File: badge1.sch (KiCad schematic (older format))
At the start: 23 parts, among them P1 CONN_01X04, P2 USB_A, P3 CONN_01X04, P4 CONN_01X03, SW1 SW_PUSH, U1 MCP1700-3302E/TO, U2 custom_logo, U3 Hillhacks_logo, U4 proto_area, U5 badge_hole2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

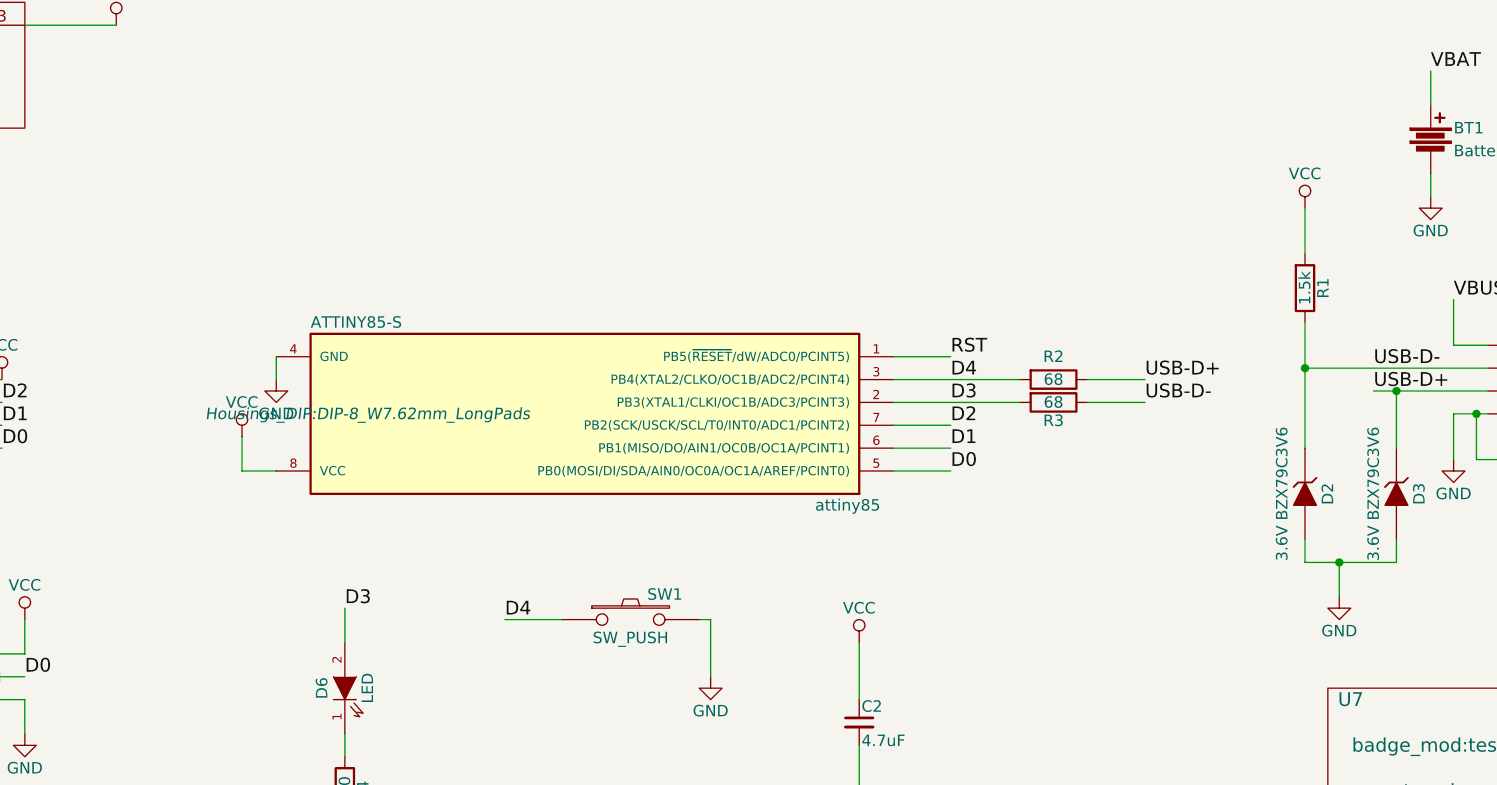
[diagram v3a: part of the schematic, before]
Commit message: fixed mistakes and made button the reset button. added more legend.
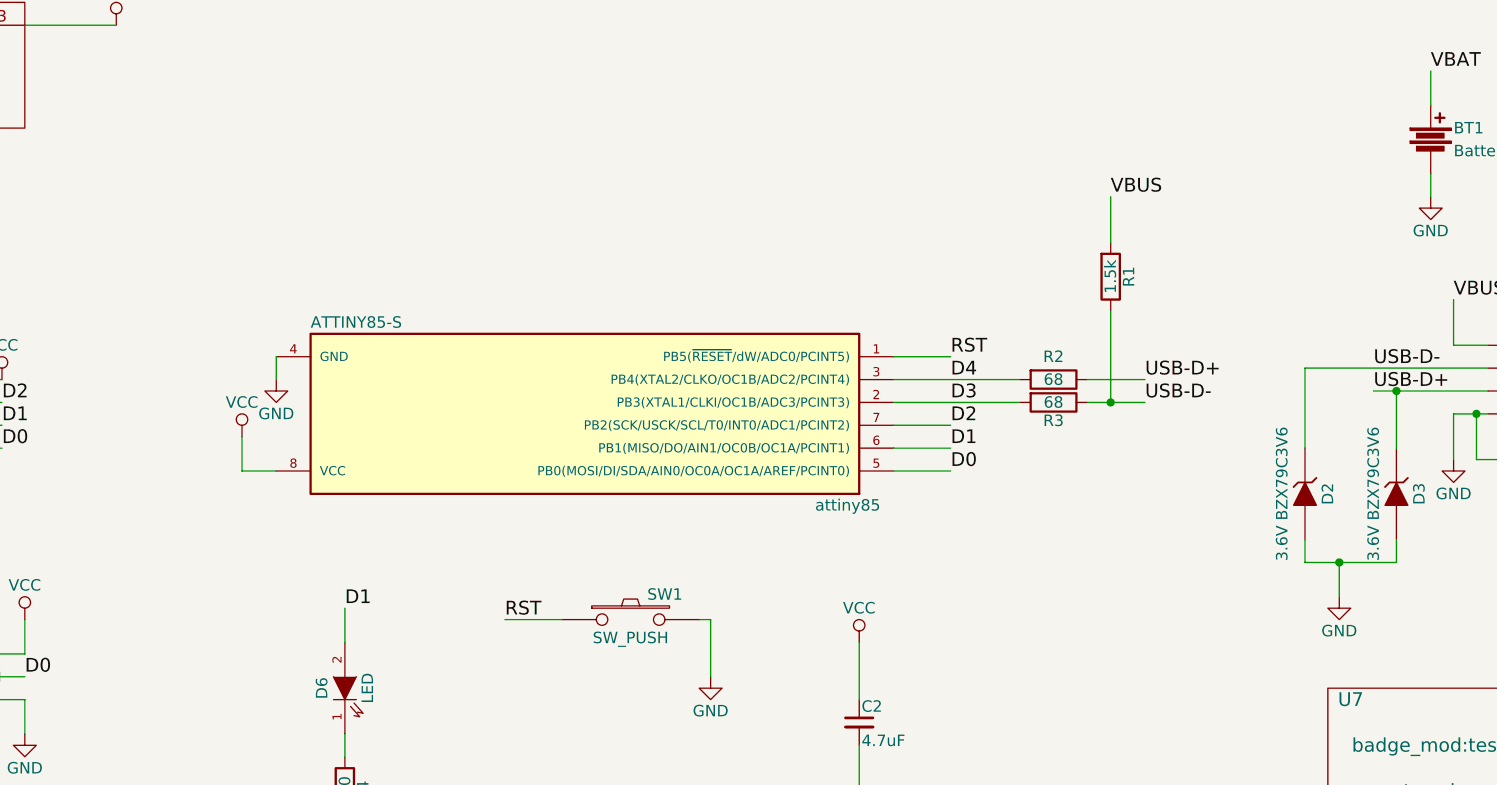
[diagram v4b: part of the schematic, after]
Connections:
- net D1: now also D6.2 (A)
- net D3: no longer D6.2 (A)
- net D4: no longer SW1.1
- net RST: now also SW1.1
- net VBUS: now also R1.2
- net VCC: no longer R1.2
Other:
- moved on the sheet: R1
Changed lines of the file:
@@
 F 0 "attiny85" H 3700 4150 50  0000 C CNN
 F 1 "ATTINY85-S" H 5850 3350 50  0000 C CNN
-F 2 "Housings_DIP:DIP-8_W7.62mm_LongPads" H 5800 3750 50  0000 C CIN
+F 2 "Housings_DIP:DIP-8_W7.62mm_LongPads" H 5800 3750 50  0001 C CIN
 F 3 "" H 4850 3750 50  0001 C CNN
 F 4 "ATTINY85-20SURCT-ND" H 4850 3750 60  0001 C CNN "digikey"
@@
 $EndComp
 Text Label 3800 4600 0    60   ~ 0
-D3
+D1
 $Comp
 L GND #PWR011
@@
 	1    0    0    -1
 $EndComp
-Text Label 4500 4650 0    60   ~ 0
-D4
 $Comp
 L SW_PUSH SW1
@@
 L R R1
 U 1 1 56D7518A
-P 8000 3200
-F 0 "R1" V 8080 3200 50  0000 C CNN
-F 1 "1.5k" V 8000 3200 50  0000 C CNN
-F 2 "Resistors_ThroughHole:Resistor_Horizontal_RM10mm" V 7930 3200 50  0001 C CNN
-F 3 "" H 8000 3200 50  0000 C CNN
-	1    8000 3200
+P 7150 3150
+F 0 "R1" V 7230 3150 50  0000 C CNN
+F 1 "1.5k" V 7150 3150 50  0000 C CNN
+F 2 "Resistors_ThroughHole:Resistor_Horizontal_RM10mm" V 7080 3150 50  0001 C CNN
+F 3 "" H 7150 3150 50  0000 C CNN
+	1    7150 3150
 	1    0    0    1
 $EndComp
-$Comp
-L VCC #PWR015
-U 1 1 56D755A1
-P 8000 2850
-F 0 "#PWR015" H 8000 2700 50  0001 C CNN
-F 1 "VCC" H 8000 3000 50  0000 C CNN
-F 2 "" H 8000 2850 50  0000 C CNN
-F 3 "" H 8000 2850 50  0000 C CNN
-	1    8000 2850
-	1    0    0    -1
-$EndComp
-Wire Wire Line
-	8000 2850 8000 3050
-Connection ~ 8000 3550
-Wire Wire Line
-	8000 4400 8000 4300
-Wire Wire Line
-	2300 3900 2100 3900
-Wire Wire Line
-	8550 2800 8550 2700
-Wire Wire Line
-	8550 2250 8550 2400
-Wire Wire Line
-	2300 3700 2100 3700
-Wire Wire Line
-	1000 3900 1200 3900
-Wire Wire Line
-	1200 3800 1000 3800
-Wire Wire Line
-	1000 3700 1200 3700
-Wire Wire Line
-	1200 3600 1000 3600
-Wire Wire Line
-	2300 3600 2100 3600
-Wire Wire Line
-	2100 3800 2300 3800
-Wire Wire Line
-	4500 4650 4750 4650
-Wire Wire Line
-	5400 4900 5400 4650
-Wire Wire Line
-	5400 4650 5350 4650
-Wire Wire Line
-	3800 5250 3800 5150
-Wire Wire Line
-	3800 5700 3800 5550
-Wire Wire Line
-	3800 4600 3800 4750
-Connection ~ 8750 3750
-Wire Wire Line
-	8750 3950 8750 3750
-Wire Wire Line
-	9200 3950 8750 3950
-Wire Wire Line
-	6050 4750 6050 5000
-Wire Wire Line
-	6050 5200 6050 5500
-Wire Wire Line
-	1150 5000 1750 5000
-Wire Wire Line
-	1150 4900 1750 4900
-Wire Wire Line
-	1150 4800 1750 4800
-Wire Wire Line
-	2400 4800 2000 4800
-Wire Wire Line
-	2400 4650 2400 4800
-Wire Wire Line
-	2400 5000 2000 5000
-Wire Wire Line
-	2400 5150 2400 5000
-Wire Wire Line
-	2400 4900 2000 4900
-Connection ~ 8400 3650
-Wire Wire Line
-	8400 3900 8400 3650
-Wire Wire Line
-	8000 3350 8000 3900
-Connection ~ 8150 4400
-Wire Wire Line
-	8400 4400 8400 4300
-Wire Wire Line
-	8150 4400 8150 4550
-Wire Wire Line
-	8000 4400 8400 4400
-Wire Wire Line
-	6200 3600 6750 3600
-Wire Wire Line
-	6200 3700 6750 3700
-Wire Wire Line
-	6450 3900 6200 3900
-Wire Wire Line
-	7300 3600 7050 3600
-Wire Wire Line
-	7300 3700 7050 3700
-Wire Wire Line
-	8300 3650 8800 3650
-Wire Wire Line
-	8000 3550 8800 3550
-Wire Wire Line
-	8650 3750 8800 3750
-Wire Wire Line
-	8650 3950 8650 3750
-Wire Wire Line
-	8650 3450 8800 3450
-Wire Wire Line
-	8650 3250 8650 3450
-Wire Wire Line
-	3500 3600 3500 3500
-Wire Wire Line
-	3350 4000 3500 4000
-Wire Wire Line
-	3350 3850 3350 4000
-Wire Wire Line
-	6450 3500 6200 3500
-Wire Wire Line
-	6200 4000 6450 4000
-Wire Wire Line
-	6450 3800 6200 3800
 $Comp
 L CONN_01X03 P4
@@
 	1    0    0    -1
 $EndComp
-Wire Wire Line
-	9900 3200 10250 3200
-Wire Wire Line
-	9900 3000 10250 3000
-Wire Wire Line
-	9500 3050 9500 3100
-Wire Wire Line
-	9500 3100 10250 3100
 $Comp
 L MCP1700-3302E/TO U1
@@
 $EndComp
 $Comp
-L VCC #PWR016
+L VCC #PWR015
 U 1 1 56D86F61
 P 2800 2050
-F 0 "#PWR016" H 2800 1900 50  0001 C CNN
+F 0 "#PWR015" H 2800 1900 50  0001 C CNN
 F 1 "VCC" H 2800 2200 50  0000 C CNN
 F 2 "" H 2800 2050 50  0000 C CNN
@@
 $EndComp
 $Comp
-L GND #PWR017
+L GND #PWR016
 U 1 1 56D86FA3
 P 2000 2650
-F 0 "#PWR017" H 2000 2400 50  0001 C CNN
+F 0 "#PWR016" H 2000 2400 50  0001 C CNN
 F 1 "GND" H 2000 2500 50  0000 C CNN
 F 2 "" H 2000 2650 50  0000 C CNN
@@
 Text Label 850  2050 0    60   ~ 0
 V_sec_bat
-Wire Wire Line
-	850  2050 1600 2050
-Wire Wire Line
-	2400 2050 2800 2050
-Wire Wire Line
-	2000 2500 2000 2650
 Text Label 1700 1050 0    60   ~ 0
 V_sec_bat
-Wire Wire Line
-	1700 1050 1600 1050
-$Comp
-L GND #PWR018
+$Comp
+L GND #PWR017
 U 1 1 56D87B87
 P 2950 1050
-F 0 "#PWR018" H 2950 800 50  0001 C CNN
+F 0 "#PWR017" H 2950 800 50  0001 C CNN
 F 1 "GND" H 2950 900 50  0000 C CNN
 F 2 "" H 2950 1050 50  0000 C CNN
@@
 	1    0    0    -1
 $EndComp
-Wire Wire Line
-	2950 1050 2700 1050
 $Comp
 L badge_hole2 U5
@@
 	1    0    0    -1
 $EndComp
+Text Label 7150 2800 0    60   ~ 0
+VBUS
+Wire Wire Line
+	7150 2800 7150 3000
+Wire Wire Line
+	8000 4400 8000 4300
+Wire Wire Line
+	2300 3900 2100 3900
+Wire Wire Line
+	8550 2800 8550 2700
+Wire Wire Line
+	8550 2250 8550 2400
+Wire Wire Line
+	2300 3700 2100 3700
+Wire Wire Line
+	1000 3900 1200 3900
+Wire Wire Line
+	1200 3800 1000 3800
+Wire Wire Line
+	1000 3700 1200 3700
+Wire Wire Line
+	1200 3600 1000 3600
+Wire Wire Line
+	2300 3600 2100 3600
+Wire Wire Line
+	2100 3800 2300 3800
+Wire Wire Line
+	4500 4650 4750 4650
+Wire Wire Line
+	5400 4900 5400 4650
+Wire Wire Line
+	5400 4650 5350 4650
+Wire Wire Line
+	3800 5250 3800 5150
+Wire Wire Line
+	3800 5700 3800 5550
+Wire Wire Line
+	3800 4600 3800 4750
+Connection ~ 8750 3750
+Wire Wire Line
+	8750 3950 8750 3750
+Wire Wire Line
+	9200 3950 8750 3950
+Wire Wire Line
+	6050 4750 6050 5000
+Wire Wire Line
+	6050 5200 6050 5500
+Wire Wire Line
+	1150 5000 1750 5000
+Wire Wire Line
+	1150 4900 1750 4900
+Wire Wire Line
+	1150 4800 1750 4800
+Wire Wire Line
+	2400 4800 2000 4800
+Wire Wire Line
+	2400 4650 2400 4800
+Wire Wire Line
+	2400 5000 2000 5000
+Wire Wire Line
+	2400 5150 2400 5000
+Wire Wire Line
+	2400 4900 2000 4900
+Connection ~ 8400 3650
+Wire Wire Line
+	8400 3900 8400 3650
+Connection ~ 8150 4400
+Wire Wire Line
+	8400 4400 8400 4300
+Wire Wire Line
+	8150 4400 8150 4550
+Wire Wire Line
+	8000 4400 8400 4400
+Wire Wire Line
+	6200 3600 6750 3600
+Wire Wire Line
+	6200 3700 6750 3700
+Wire Wire Line
+	6450 3900 6200 3900
+Wire Wire Line
+	7300 3600 7050 3600
+Wire Wire Line
+	7300 3700 7050 3700
+Wire Wire Line
+	8300 3650 8800 3650
+Wire Wire Line
+	8000 3550 8800 3550
+Wire Wire Line
+	8650 3750 8800 3750
+Wire Wire Line
+	8650 3950 8650 3750
+Wire Wire Line
+	8650 3450 8800 3450
+Wire Wire Line
+	8650 3250 8650 3450
+Wire Wire Line
+	3500 3600 3500 3500
+Wire Wire Line
+	3350 4000 3500 4000
+Wire Wire Line
+	3350 3850 3350 4000
+Wire Wire Line
+	6450 3500 6200 3500
+Wire Wire Line
+	6200 4000 6450 4000
+Wire Wire Line
+	6450 3800 6200 3800
+Wire Wire Line
+	9900 3200 10250 3200
+Wire Wire Line
+	9900 3000 10250 3000
+Wire Wire Line
+	9500 3050 9500 3100
+Wire Wire Line
+	9500 3100 10250 3100
+Wire Wire Line
+	850  2050 1600 2050
+Wire Wire Line
+	2400 2050 2800 2050
+Wire Wire Line
+	2000 2500 2000 2650
+Wire Wire Line
+	1700 1050 1600 1050
+Wire Wire Line
+	2950 1050 2700 1050
+Wire Wire Line
+	8000 3550 8000 3900
+Wire Wire Line
+	7150 3700 7150 3300
+Connection ~ 7150 3700
+Text Label 4500 4650 0    60   ~ 0
+RST
 $EndSCHEMATC

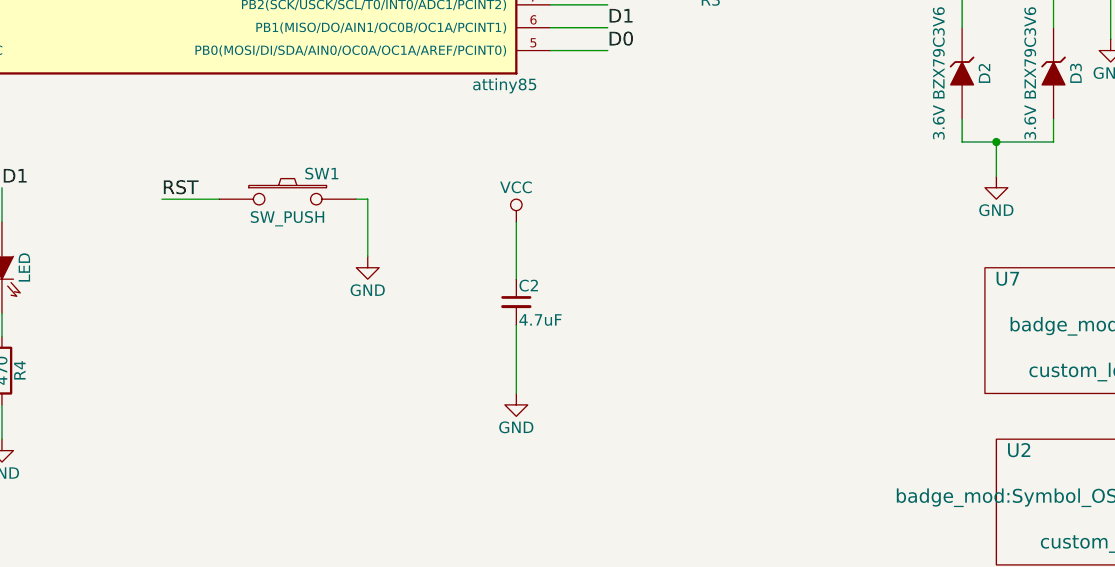
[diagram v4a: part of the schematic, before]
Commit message: Update schematic/layout with fixes. Update readme for small howto.
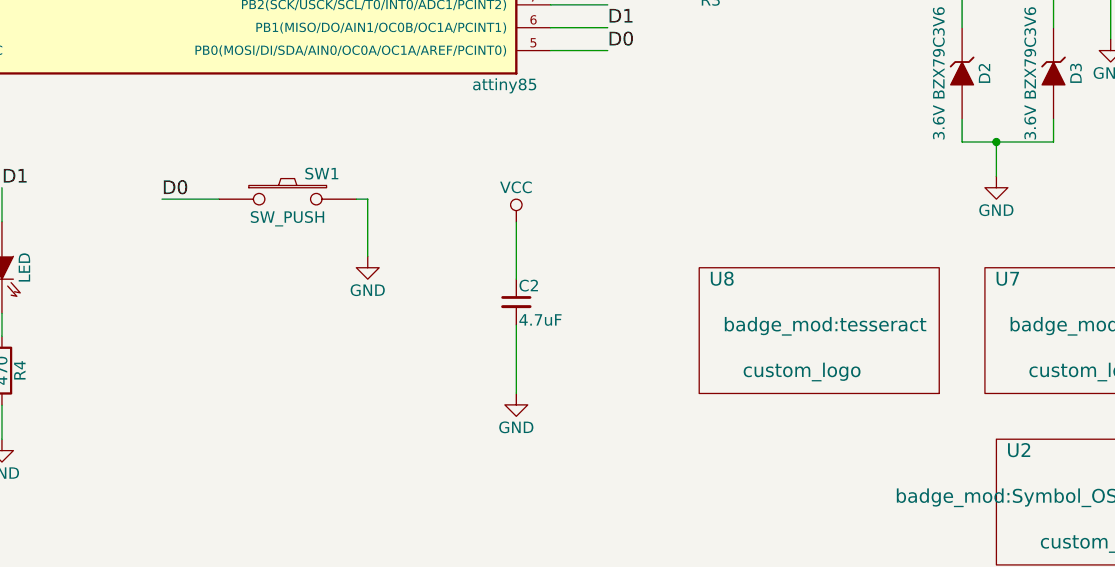
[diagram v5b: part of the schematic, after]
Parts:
- added U8: custom_logo, badge_mod:tesseract, symbol custom_logo
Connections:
- net D0: now also SW1.1
- net RST: no longer SW1.1
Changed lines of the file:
@@
 Connection ~ 7150 3700
 Text Label 4500 4650 0    60   ~ 0
-RST
+D0
+$Comp
+L custom_logo U8
+U 1 1 570A1F46
+P 7400 5200
+F 0 "U8" H 6950 5400 60  0000 C CNN
+F 1 "custom_logo" H 7300 5000 60  0000 C CNN
+F 2 "badge_mod:tesseract" H 7400 5200 60  0000 C CNN
+F 3 "" H 7400 5200 60  0000 C CNN
+	1    7400 5200
+	1    0    0    -1
+$EndComp
 $EndSCHEMATC
